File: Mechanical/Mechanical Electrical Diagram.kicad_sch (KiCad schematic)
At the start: 12 parts, among them U12 Spark MAX Motor Controller, U16 Spark MAX Motor Controller, U20 Spark MAX Motor Controller, U24 Rev Neo, U25 Rev Neo, U26 Rev Neo, U27 Rev Neo, U3 Rev Neo, U5 Spark MAX Motor Controller, U6 Spark MAX Motor Controller

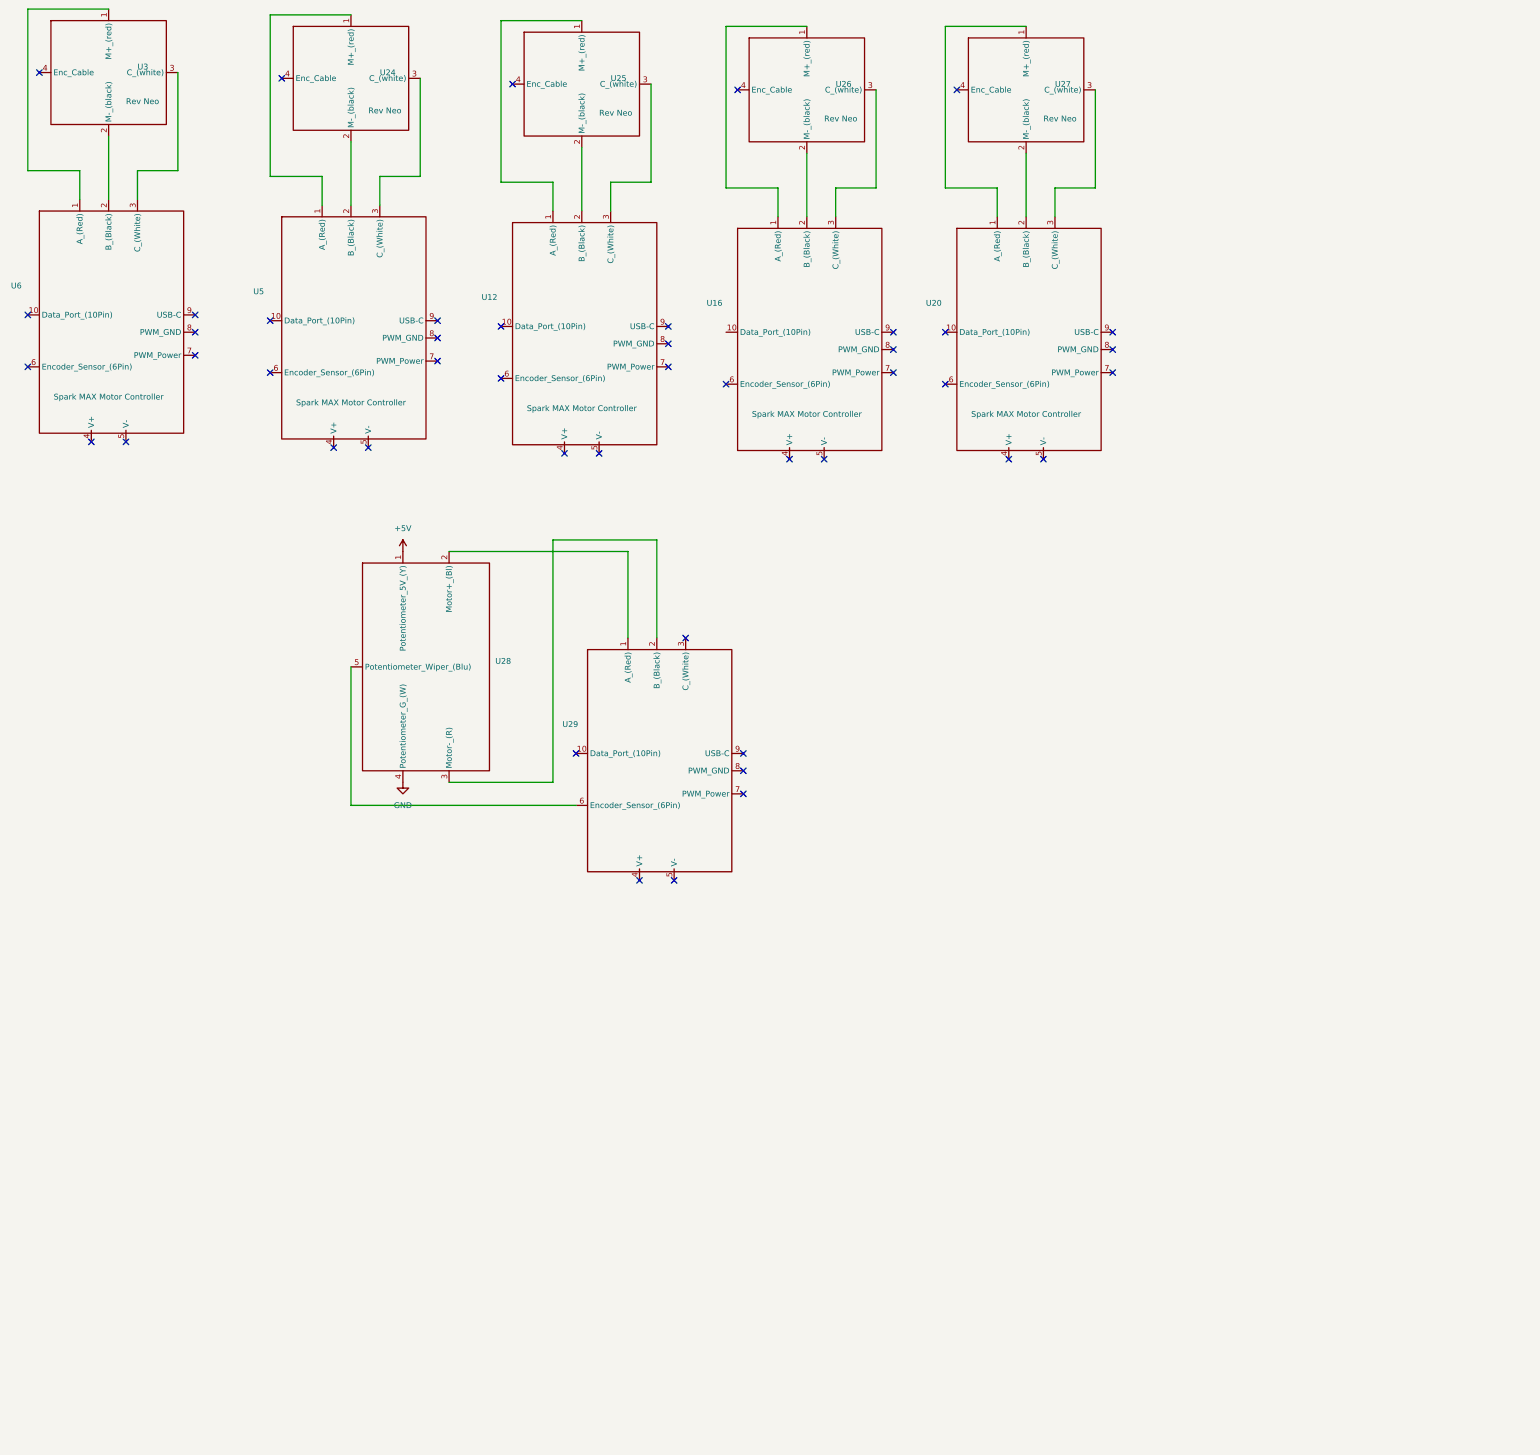
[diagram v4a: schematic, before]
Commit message: Finalized Schematics with linear actuator and updated encoder
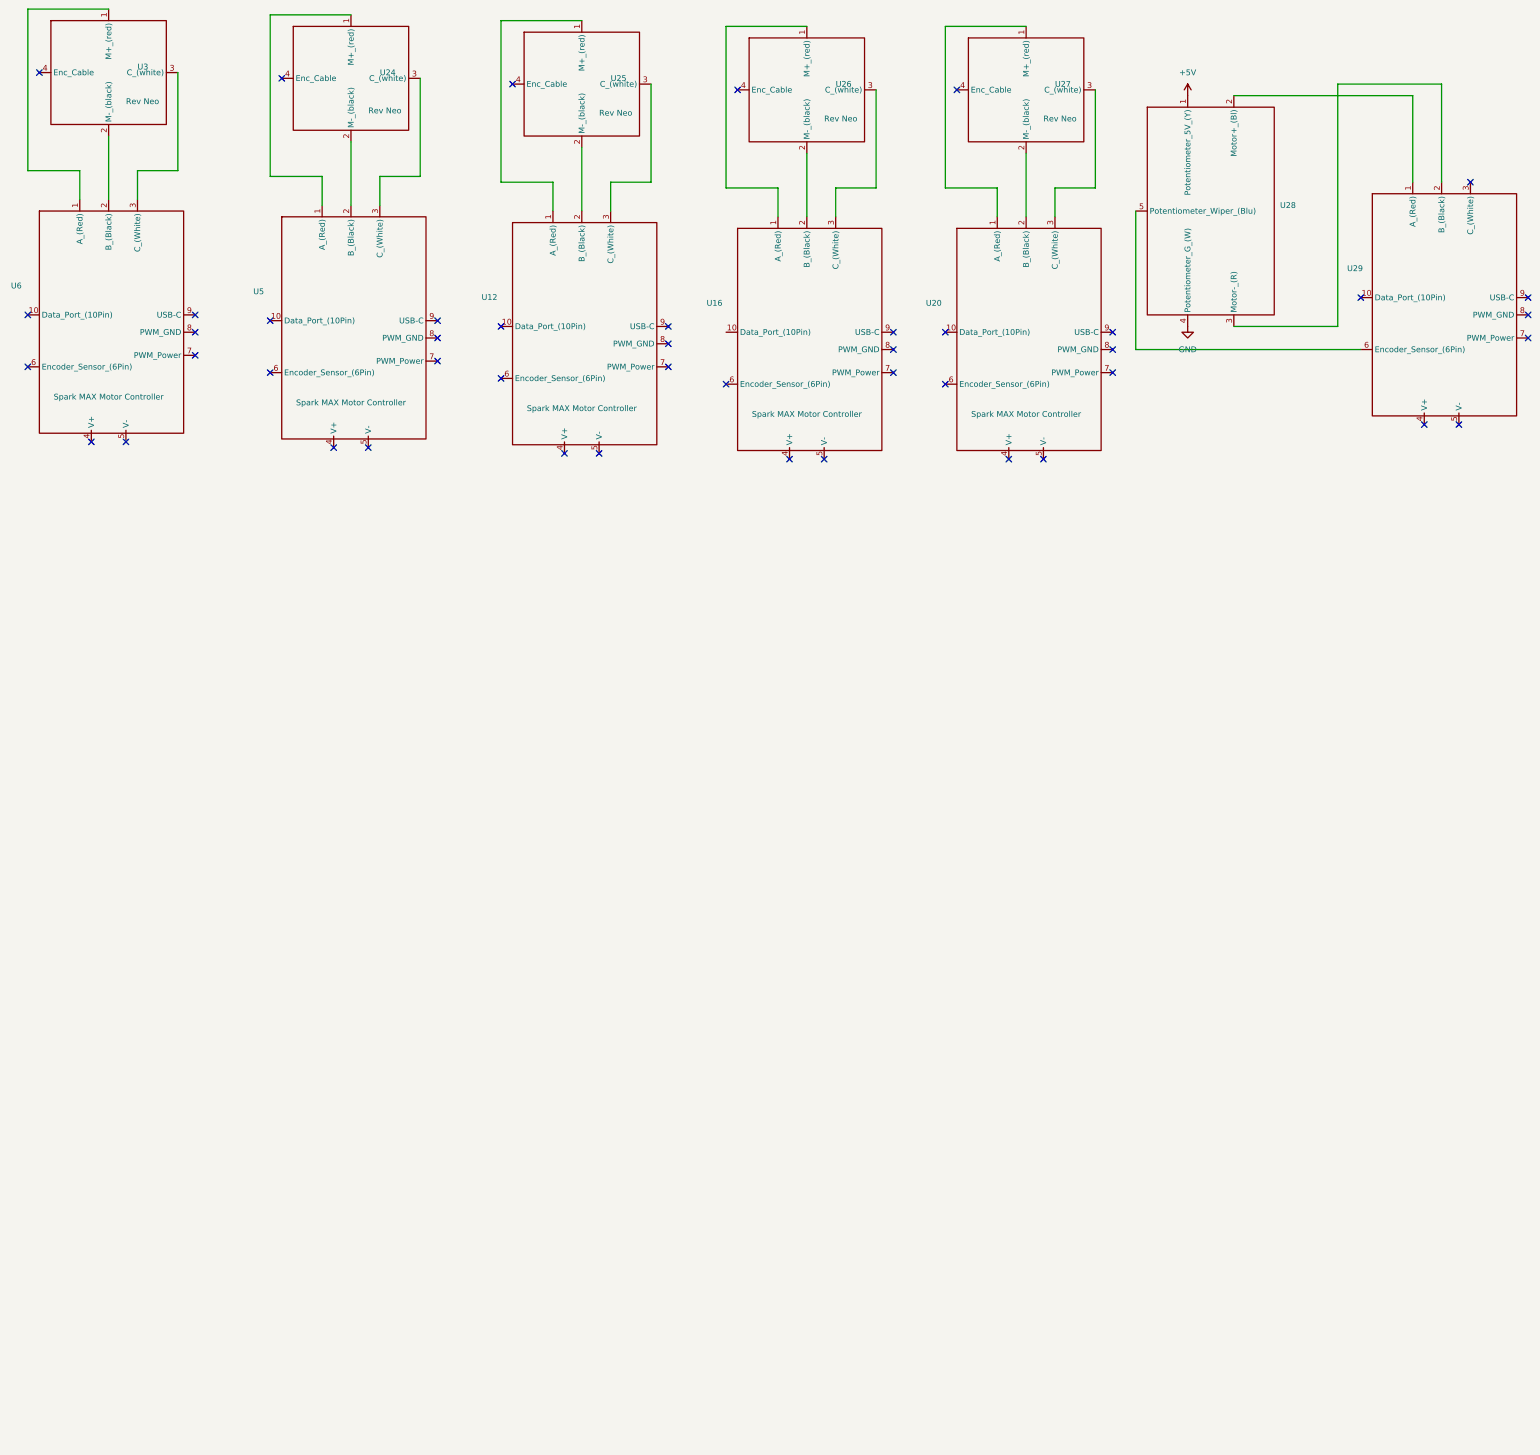
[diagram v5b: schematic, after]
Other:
- moved on the sheet: U28, U29
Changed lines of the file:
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@@
 	)
 	(no_connect
-		(at 187.96 209.55)
+		(at 360.68 109.22)
 	)
 	(no_connect
@@
 	)
 	(no_connect
-		(at 187.96 214.63)
+		(at 360.68 114.3)
 	)
 	(no_connect
@@
 	)
 	(no_connect
-		(at 187.96 205.74)
+		(at 360.68 105.41)
 	)
 	(no_connect
@@
 	)
 	(no_connect
-		(at 172.72 233.68)
-	)
-	(no_connect
-		(at 175.26 180.34)
-	)
-	(no_connect
-		(at 151.13 205.74)
+		(at 345.44 133.35)
+	)
+	(no_connect
+		(at 347.98 80.01)
+	)
+	(no_connect
+		(at 323.85 105.41)
 	)
 	(no_connect
@@
 	)
 	(no_connect
-		(at 165.1 233.68)
+		(at 337.82 133.35)
 	)
 	(no_connect
@@
 	(wire
 		(pts
-			(xy 168.91 180.34) (xy 168.91 158.75)
+			(xy 341.63 80.01) (xy 341.63 58.42)
 		)
 		(stroke
@@
 	(wire
 		(pts
-			(xy 101.6 186.69) (xy 101.6 217.17)
+			(xy 274.32 86.36) (xy 274.32 116.84)
 		)
 		(stroke
@@
 	(wire
 		(pts
-			(xy 123.19 161.29) (xy 162.56 161.29)
+			(xy 295.91 60.96) (xy 335.28 60.96)
 		)
 		(stroke
@@
 	(wire
 		(pts
-			(xy 162.56 180.34) (xy 162.56 161.29)
+			(xy 335.28 80.01) (xy 335.28 60.96)
 		)
 		(stroke
@@
 	(wire
 		(pts
-			(xy 146.05 158.75) (xy 146.05 212.09)
+			(xy 318.77 58.42) (xy 318.77 111.76)
 		)
 		(stroke
@@
 	(wire
 		(pts
-			(xy 146.05 212.09) (xy 123.19 212.09)
+			(xy 318.77 111.76) (xy 295.91 111.76)
 		)
 		(stroke
@@
 	(wire
 		(pts
-			(xy 101.6 217.17) (xy 151.13 217.17)
-		)
-		(stroke
-			(width 0)
-			(type default)
-		)
-	)
-	(wire
-		(pts
-			(xy 168.91 158.75) (xy 146.05 158.75)
+			(xy 274.32 116.84) (xy 323.85 116.84)
+		)
+		(stroke
+			(width 0)
+			(type default)
+		)
+	)
+	(wire
+		(pts
+			(xy 341.63 58.42) (xy 318.77 58.42)
 		)
 		(stroke
@@
 	(symbol
 		(lib_id "power:+5V")
-		(at 113.03 161.29 0)
+		(at 285.75 60.96 0)
 		(unit 1)
 		(exclude_from_sim no)
@@
 		(fields_autoplaced yes)
 		(property "Reference" "#PWR03"
-			(at 113.03 165.1 0)
+			(at 285.75 64.77 0)
 			(effects
 				(font
@@
 		)
 		(property "Value" "+5V"
-			(at 113.03 156.21 0)
+			(at 285.75 55.88 0)
 			(effects
 				(font
@@
 		)
 		(property "Footprint" ""
-			(at 113.03 161.29 0)
+			(at 285.75 60.96 0)
 			(effects
 				(font
@@
 		)
 		(property "Datasheet" ""
-			(at 113.03 161.29 0)
+			(at 285.75 60.96 0)
 			(effects
 				(font
@@
 		)
 		(property "Description" "Power symbol creates a global label with name \"+5V\""
-			(at 113.03 161.29 0)
+			(at 285.75 60.96 0)
 			(effects
 				(font
@@
 	(symbol
 		(lib_id "Lunabotics 2025-26:Feedback_Linear_Actuator")
-		(at 118.11 186.69 0)
+		(at 290.83 86.36 0)
 		(unit 1)
 		(exclude_from_sim no)
@@
 		(fields_autoplaced yes)
 		(property "Reference" "U28"
-			(at 133.35 185.4199 0)
+			(at 306.07 85.0899 0)
 			(effects
 				(font
@@
 		)
 		(property "Value" "~"
-			(at 133.35 187.9599 0)
+			(at 306.07 87.6299 0)
 			(effects
 				(font
@@
 		)
 		(property "Footprint" ""
-			(at 118.11 186.69 0)
+			(at 290.83 86.36 0)
 			(effects
 				(font
@@
 		)
 		(property "Datasheet" ""
-			(at 118.11 186.69 0)
+			(at 290.83 86.36 0)
 			(effects
 				(font
@@
 		)
 		(property "Description" ""
-			(at 118.11 186.69 0)
+			(at 290.83 86.36 0)
 			(effects
 				(font
@@
 		(lib_name "Spark_MAX_Motor_Controller_1")
 		(lib_id "Lunabotics 2025-26:Spark_MAX_Motor_Controller")
-		(at 168.91 212.09 0)
+		(at 341.63 111.76 0)
 		(unit 1)
 		(exclude_from_sim no)
@@
 		(fields_autoplaced yes)
 		(property "Reference" "U29"
-			(at 149.86 199.3198 0)
+			(at 322.58 98.9898 0)
 			(effects
 				(font
@@
 		)
 		(property "Value" "~"
-			(at 149.86 201.8598 0)
+			(at 322.58 101.5298 0)
 			(effects
 				(font
@@
 		)
 		(property "Footprint" ""
-			(at 168.91 212.09 0)
+			(at 341.63 111.76 0)
 			(effects
 				(font
@@
 		)
 		(property "Datasheet" ""
-			(at 168.91 212.09 0)
+			(at 341.63 111.76 0)
 			(effects
 				(font
@@
 		)
 		(property "Description" ""
-			(at 168.91 212.09 0)
+			(at 341.63 111.76 0)
 			(effects
 				(font
@@
 	(symbol
 		(lib_id "power:GND")
-		(at 113.03 212.09 0)
+		(at 285.75 111.76 0)
 		(unit 1)
 		(exclude_from_sim no)
@@
 		(fields_autoplaced yes)
 		(property "Reference" "#PWR05"
-			(at 113.03 218.44 0)
+			(at 285.75 118.11 0)
 			(effects
 				(font
@@
 		)
 		(property "Value" "GND"
-			(at 113.03 217.17 0)
+			(at 285.75 116.84 0)
 			(effects
 				(font
@@
 		)
 		(property "Footprint" ""
-			(at 113.03 212.09 0)
+			(at 285.75 111.76 0)
 			(effects
 				(font
@@
 		)
 		(property "Datasheet" ""
-			(at 113.03 212.09 0)
+			(at 285.75 111.76 0)
 			(effects
 				(font
@@
 		)
 		(property "Description" "Power symbol creates a global label with name \"GND\" , ground"
-			(at 113.03 212.09 0)
-			(effects
-				(font
+			(at 285.75 111.76 0)
+			(effects
+				(font

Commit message: Updated Schematics & Library
Added Alternate Encoder to library and schematics, allows correct connection for Spark MAX to Neos. Also removed incorrect connection of linear actuator "encoder" to Spark MAX.
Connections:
- net at U28.5 (Potentiometer_Wiper_(Blu)): no longer U29.6 (Encoder_Sensor_(6Pin))
- no-connect marks 46 -> 47
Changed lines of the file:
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@@
+	)
+	(no_connect
+		(at 274.32 86.36)
 	)
 	(no_connect
@@
 	(wire
 		(pts
-			(xy 274.32 86.36) (xy 274.32 116.84)
-		)
-		(stroke
-			(width 0)
-			(type default)
-		)
-	)
-	(wire
-		(pts
 			(xy 54.61 83.82) (xy 54.61 77.47)
 		)
@@
 		)
 		(stroke
-			(width 0)
-			(type default)
-		)
-	)
-	(wire
-		(pts
-			(xy 274.32 116.84) (xy 323.85 116.84)
-		)
-		(stroke

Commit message: Refreshed changed symbols in Mech & Power Schematics
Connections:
- no-connect marks 47 -> 59
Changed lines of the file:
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@@
+	)
+	(no_connect
+		(at 269.24 127)
 	)
 	(no_connect
@@
 	)
 	(no_connect
+		(at 269.24 130.81)
+	)
+	(no_connect
+		(at 120.65 124.46)
+	)
+	(no_connect
 		(at 120.65 119.38)
 	)
 	(no_connect
+		(at 360.68 123.19)
+	)
+	(no_connect
 		(at 232.41 113.03)
 	)
 	(no_connect
+		(at 220.98 127)
+	)
+	(no_connect
 		(at 148.59 139.7)
 	)
@@
 	)
 	(no_connect
+		(at 171.45 125.73)
+	)
+	(no_connect
 		(at 220.98 121.92)
 	)
 	(no_connect
+		(at 67.31 123.19)
+	)
+	(no_connect
 		(at 30.48 109.22)
 	)
 	(no_connect
+		(at 360.68 119.38)
+	)
+	(no_connect
+		(at 171.45 129.54)
+	)
+	(no_connect
 		(at 360.68 114.3)
 	)
@@
 	)
 	(no_connect
+		(at 67.31 127)
+	)
+	(no_connect
 		(at 360.68 105.41)
 	)
@@
 	)
 	(no_connect
+		(at 220.98 130.81)
+	)
+	(no_connect
 		(at 44.45 137.16)
 	)
@@
 	(no_connect
 		(at 274.32 86.36)
+	)
+	(no_connect
+		(at 120.65 128.27)
 	)
 	(no_connect
@@
 		(pin "9"
 		)
+		(pin "12"
+		)
+		(pin "11"
+		)
 		(instances
 			(project "Mechanical Electrical Diagram"
@@
 		)
 		(pin "9"
+		)
+		(pin "11"
+		)
+		(pin "12"
 		)
 		(instances
@@
 	)
 	(symbol
-		(lib_name "Spark_MAX_Motor_Controller_1")
 		(lib_id "Lunabotics 2025-26:Spark_MAX_Motor_Controller")
 		(at 341.63 111.76 0)
@@
 		(pin "5"
 		)
+		(pin "12"
+		)
+		(pin "11"
+		)
 		(instances
 			(project "Mechanical Electrical Diagram"
@@
 		(pin "9"
 		)
+		(pin "12"
+		)
+		(pin "11"
+		)
 		(instances
 			(project "Mechanical Electrical Diagram"
@@
 		(pin "9"
 		)
+		(pin "11"
+		)
+		(pin "12"
+		)
 		(instances
 			(project "Mechanical Electrical Diagram"
@@
 		(pin "9"
 		)
+		(pin "11"
+		)
+		(pin "12"
+		)
 		(instances
